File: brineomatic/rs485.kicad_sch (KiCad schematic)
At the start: 12 parts, among them J23 3.5mm, J24 3.5mm, U10 MAX3485

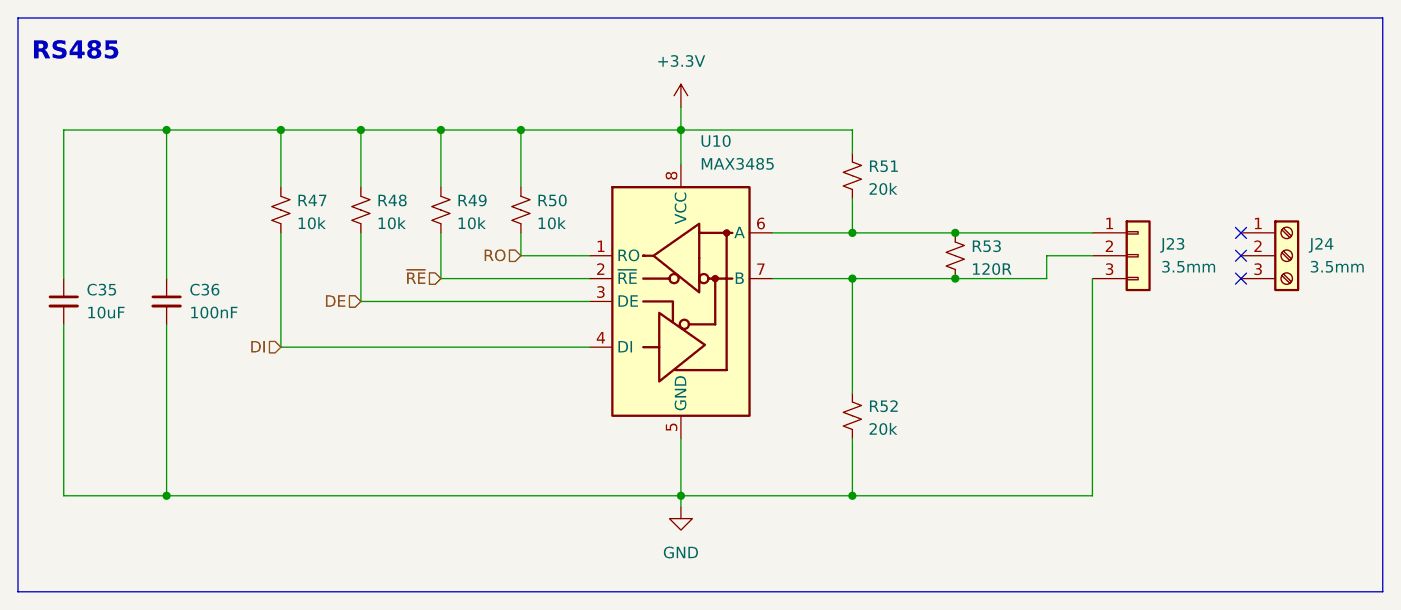
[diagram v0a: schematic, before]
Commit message: switch to rt7272b for 24v -> 5v regulator
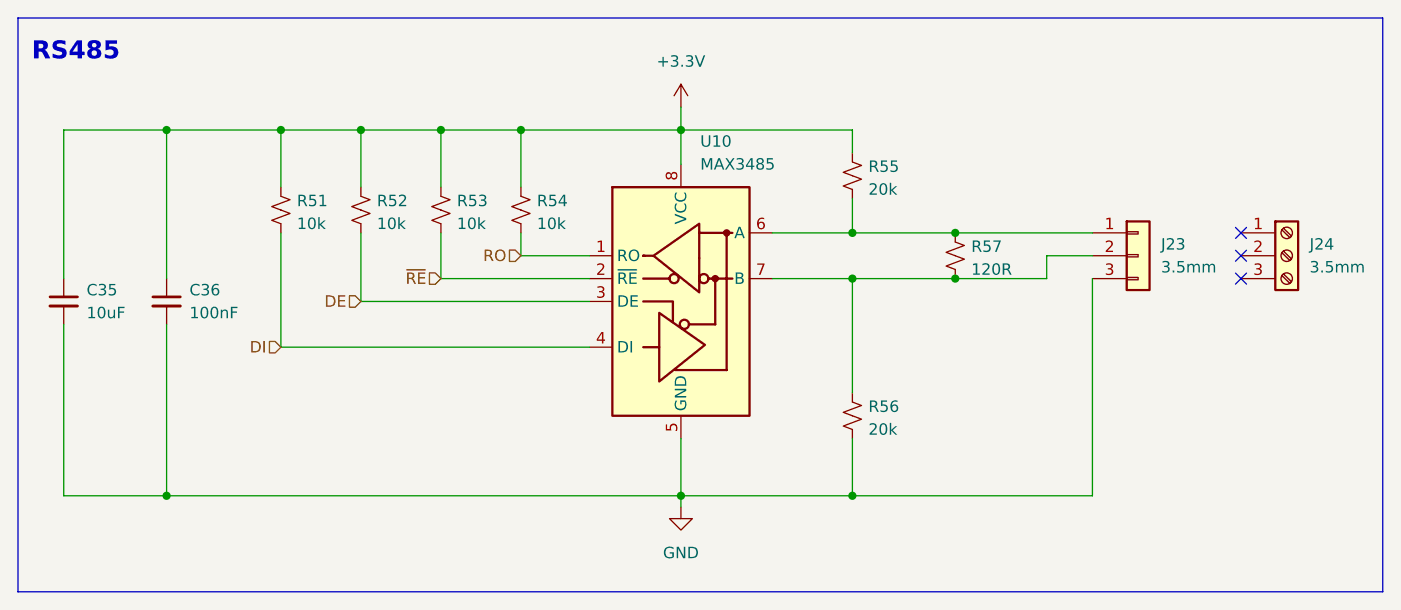
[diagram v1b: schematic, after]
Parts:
- renumbered R47 to R51, R48 to R52, R49 to R53, R50 to R54, R51 to R55, R52 to R56, R53 to R57
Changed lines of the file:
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@@
 		(dnp no)
 		(fields_autoplaced yes)
-		(property "Reference" "#PWR070"
+		(property "Reference" "#PWR068"
 			(at 140.97 130.81 0)
 			(effects
@@
 			(project "brineomatic"
 				(path "/96477ae2-ef08-48f3-8dd4-fe4478541f68/ecabf60a-7f79-4ba0-9fc6-a1e702c2d5f0"
-					(reference "#PWR070")
+					(reference "#PWR068")
 					(unit 1)
 				)
@@
 		(on_board yes)
 		(dnp no)
-		(property "Reference" "R52"
+		(property "Reference" "R56"
 			(at 161.798 113.284 0)
 			(effects
@@
 			(project "brineomatic"
 				(path "/96477ae2-ef08-48f3-8dd4-fe4478541f68/ecabf60a-7f79-4ba0-9fc6-a1e702c2d5f0"
-					(reference "R52")
+					(reference "R56")
 					(unit 1)
 				)
@@
 		(on_board yes)
 		(dnp no)
-		(property "Reference" "R47"
+		(property "Reference" "R51"
 			(at 98.298 90.424 0)
 			(effects
@@
 			(project "brineomatic"
 				(path "/96477ae2-ef08-48f3-8dd4-fe4478541f68/ecabf60a-7f79-4ba0-9fc6-a1e702c2d5f0"
-					(reference "R47")
+					(reference "R51")
 					(unit 1)
 				)
@@
 		(on_board yes)
 		(dnp no)
-		(property "Reference" "R49"
+		(property "Reference" "R53"
 			(at 116.078 90.424 0)
 			(effects
@@
 			(project "brineomatic"
 				(path "/96477ae2-ef08-48f3-8dd4-fe4478541f68/ecabf60a-7f79-4ba0-9fc6-a1e702c2d5f0"
-					(reference "R49")
+					(reference "R53")
 					(unit 1)
 				)
@@
 		(on_board yes)
 		(dnp no)
-		(property "Reference" "R50"
+		(property "Reference" "R54"
 			(at 124.968 90.424 0)
 			(effects
@@
 			(project "brineomatic"
 				(path "/96477ae2-ef08-48f3-8dd4-fe4478541f68/ecabf60a-7f79-4ba0-9fc6-a1e702c2d5f0"
-					(reference "R50")
+					(reference "R54")
 					(unit 1)
 				)
@@
 		(on_board yes)
 		(dnp no)
-		(property "Reference" "R53"
+		(property "Reference" "R57"
 			(at 173.228 95.504 0)
 			(effects
@@
 			(project "brineomatic"
 				(path "/96477ae2-ef08-48f3-8dd4-fe4478541f68/ecabf60a-7f79-4ba0-9fc6-a1e702c2d5f0"
-					(reference "R53")
+					(reference "R57")
 					(unit 1)
 				)
@@
 		(dnp no)
 		(fields_autoplaced yes)
-		(property "Reference" "#PWR069"
+		(property "Reference" "#PWR067"
 			(at 140.97 83.82 0)
 			(effects
@@
 			(project ""
 				(path "/96477ae2-ef08-48f3-8dd4-fe4478541f68/ecabf60a-7f79-4ba0-9fc6-a1e702c2d5f0"
-					(reference "#PWR069")
+					(reference "#PWR067")
 					(unit 1)
 				)
@@
 		(on_board yes)
 		(dnp no)
-		(property "Reference" "R48"
+		(property "Reference" "R52"
 			(at 107.188 90.424 0)
 			(effects
@@
 			(project "brineomatic"
 				(path "/96477ae2-ef08-48f3-8dd4-fe4478541f68/ecabf60a-7f79-4ba0-9fc6-a1e702c2d5f0"
-					(reference "R48")
+					(reference "R52")
 					(unit 1)
 				)
@@
 		(on_board yes)
 		(dnp no)
-		(property "Reference" "R51"
+		(property "Reference" "R55"
 			(at 161.798 86.614 0)
 			(effects
@@
 			(project "brineomatic"
 				(path "/96477ae2-ef08-48f3-8dd4-fe4478541f68/ecabf60a-7f79-4ba0-9fc6-a1e702c2d5f0"
-					(reference "R51")
-					(unit 1)
-				)
+					(reference "R55")
+					(unit 1)
+				)

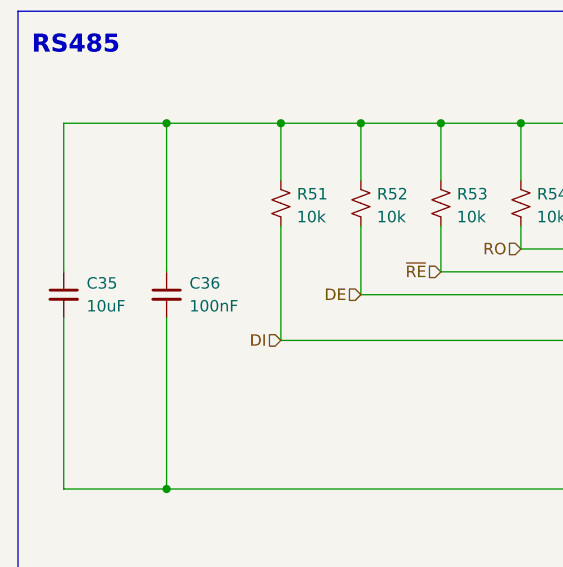
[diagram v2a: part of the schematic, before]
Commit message: added bulk cap to 5v rail and tidied silkscreen
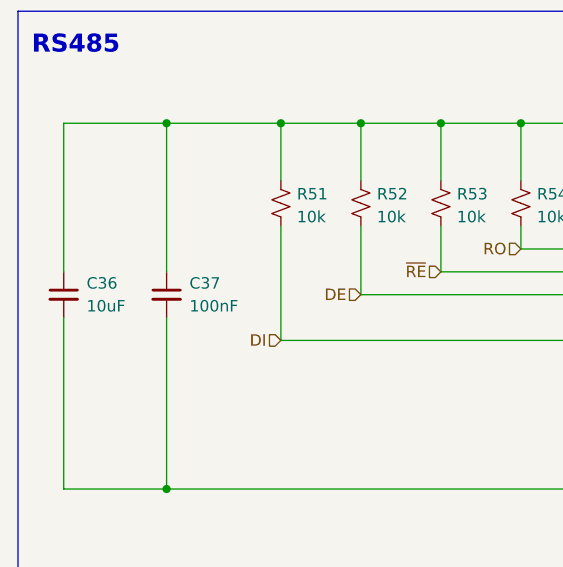
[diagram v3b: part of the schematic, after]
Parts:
- renumbered C35 to C36, C36 to C37
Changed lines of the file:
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@@
 		(on_board yes)
 		(dnp no)
-		(property "Reference" "C35"
+		(property "Reference" "C36"
 			(at 74.93 100.3363 0)
 			(effects
@@
 			(project "brineomatic"
 				(path "/96477ae2-ef08-48f3-8dd4-fe4478541f68/ecabf60a-7f79-4ba0-9fc6-a1e702c2d5f0"
-					(reference "C35")
+					(reference "C36")
 					(unit 1)
 				)
@@
 		(dnp no)
 		(fields_autoplaced yes)
-		(property "Reference" "C36"
+		(property "Reference" "C37"
 			(at 86.36 100.3363 0)
 			(effects
@@
 			(project "brineomatic"
 				(path "/96477ae2-ef08-48f3-8dd4-fe4478541f68/ecabf60a-7f79-4ba0-9fc6-a1e702c2d5f0"
-					(reference "C36")
-					(unit 1)
-				)
+					(reference "C37")
+					(unit 1)
+				)

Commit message: tested and update bom + placement
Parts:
- C37: LCSC (none) -> C14663
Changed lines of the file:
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@@
 			)
 		)
-		(property "LCSC" ""
+		(property "LCSC" "C14663"
 			(at 83.82 101.6 0)
 			(effects

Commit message: updated resistor p/ns in bom
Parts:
- R51, R52, R53, R54: LCSC (none) -> C25804
- R55, R56: LCSC (none) -> C4184
- R57: LCSC (none) -> C22787
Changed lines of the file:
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@@
+			)
+		)
+		(property "LCSC" " C4184"
+			(at 160.02 114.3 0)
+			(effects
+				(font
+					(size 1.27 1.27)
+				)
+				(hide yes)
 			)
 		)
@@
 			)
 		)
+		(property "LCSC" "C25804"
+			(at 96.52 91.44 0)
+			(effects
+				(font
+					(size 1.27 1.27)
+				)
+				(hide yes)
+			)
+		)
 		(pin "1"
 		)
@@
 			)
 		)
+		(property "LCSC" "C25804"
+			(at 114.3 91.44 0)
+			(effects
+				(font
+					(size 1.27 1.27)
+				)
+				(hide yes)
+			)
+		)
 		(pin "1"
 		)
@@
 			)
 		)
+		(property "LCSC" "C25804"
+			(at 123.19 91.44 0)
+			(effects
+				(font
+					(size 1.27 1.27)
+				)
+				(hide yes)
+			)
+		)
 		(pin "1"
 		)
@@
 		)
 		(property "Description" "Resistor, small US symbol"
+			(at 171.45 96.52 0)
+			(effects
+				(font
+					(size 1.27 1.27)
+				)
+				(hide yes)
+			)
+		)
+		(property "LCSC" " C22787"
 			(at 171.45 96.52 0)
 			(effects
@@
 			)
 		)
+		(property "LCSC" "C25804"
+			(at 105.41 91.44 0)
+			(effects
+				(font
+					(size 1.27 1.27)
+				)
+				(hide yes)
+			)
+		)
 		(pin "1"
 		)
@@
 			(at 160.02 87.63 0)
 			(effects
+				(font
+					(size 1.27 1.27)
+				)
+				(hide yes)
+			)
+		)
+		(property "LCSC" " C4184"
+			(at 160.02 87.63 0)
+			(effects

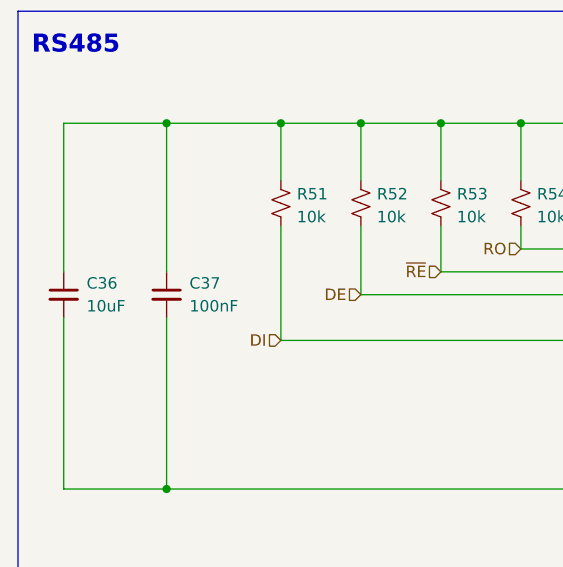
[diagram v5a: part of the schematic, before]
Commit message: added esd protection to relay driver connector
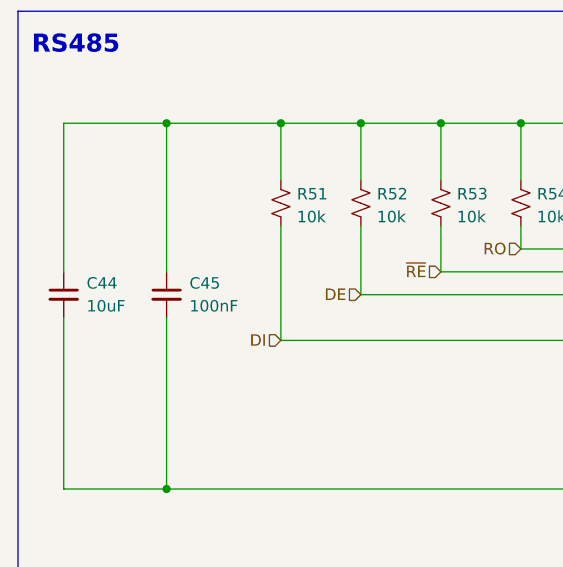
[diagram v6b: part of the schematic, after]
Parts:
- renumbered C36 to C44, C37 to C45
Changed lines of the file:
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@@
 		(on_board yes)
 		(dnp no)
-		(property "Reference" "C36"
+		(property "Reference" "C44"
 			(at 74.93 100.3363 0)
 			(effects
@@
 			(project "brineomatic"
 				(path "/96477ae2-ef08-48f3-8dd4-fe4478541f68/ecabf60a-7f79-4ba0-9fc6-a1e702c2d5f0"
-					(reference "C36")
+					(reference "C44")
 					(unit 1)
 				)
@@
 		(dnp no)
 		(fields_autoplaced yes)
-		(property "Reference" "C37"
+		(property "Reference" "C45"
 			(at 86.36 100.3363 0)
 			(effects
@@
 			(project "brineomatic"
 				(path "/96477ae2-ef08-48f3-8dd4-fe4478541f68/ecabf60a-7f79-4ba0-9fc6-a1e702c2d5f0"
-					(reference "C37")
-					(unit 1)
-				)
+					(reference "C45")
+					(unit 1)
+				)

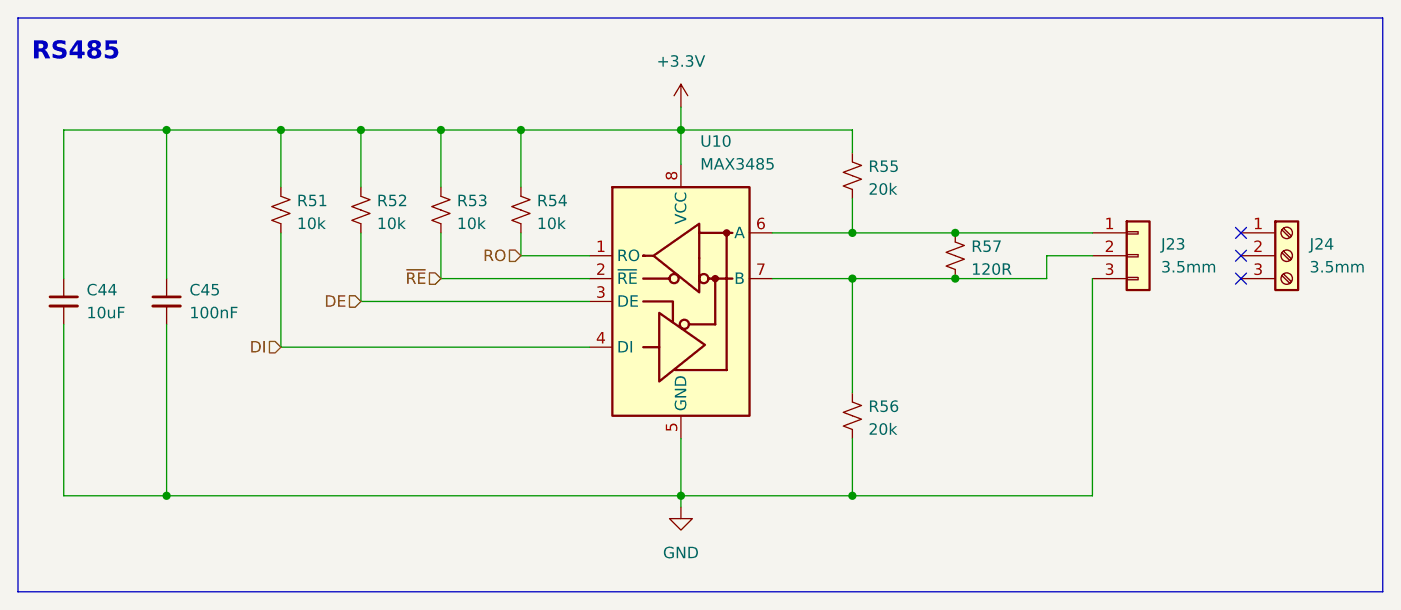
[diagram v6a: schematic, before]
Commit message: put 2x0 ohm between GND and USB SHIELD
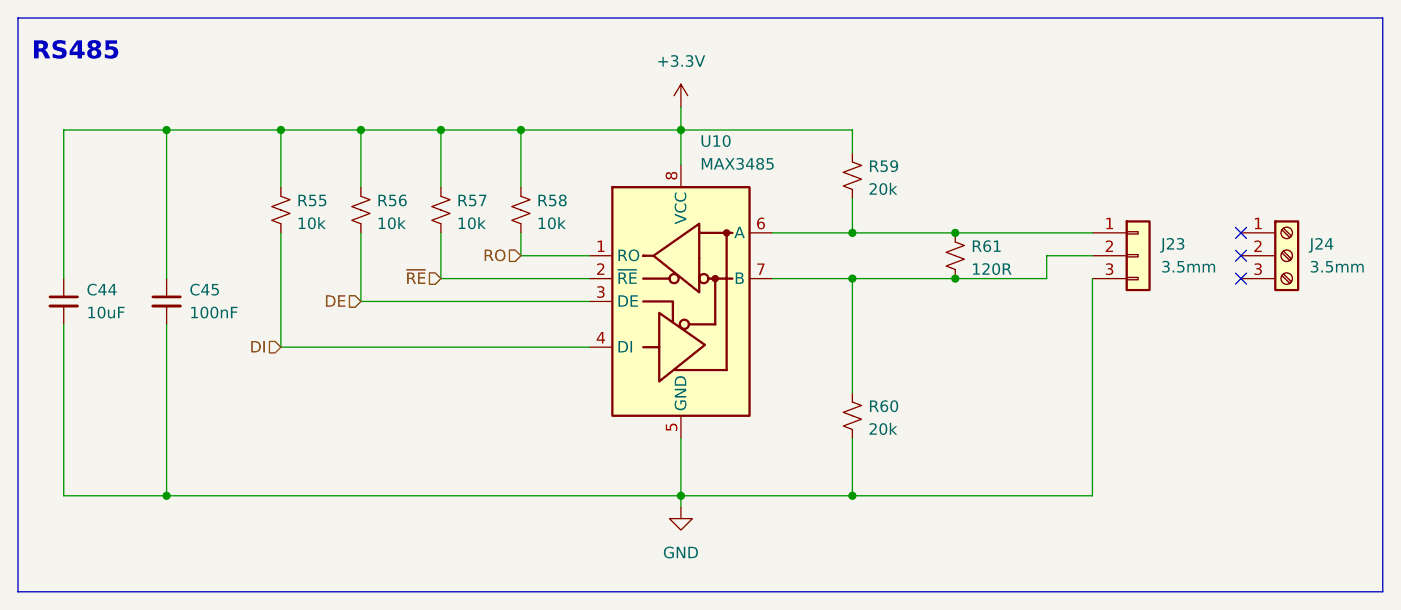
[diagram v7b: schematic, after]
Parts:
- renumbered R51 to R55, R52 to R56, R53 to R57, R54 to R58, R55 to R59, R56 to R60, R57 to R61
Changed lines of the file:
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@@
 		(on_board yes)
 		(dnp no)
-		(property "Reference" "R56"
+		(property "Reference" "R60"
 			(at 161.798 113.284 0)
 			(effects
@@
 			(project "brineomatic"
 				(path "/96477ae2-ef08-48f3-8dd4-fe4478541f68/ecabf60a-7f79-4ba0-9fc6-a1e702c2d5f0"
-					(reference "R56")
+					(reference "R60")
 					(unit 1)
 				)
@@
 		(on_board yes)
 		(dnp no)
-		(property "Reference" "R51"
+		(property "Reference" "R55"
 			(at 98.298 90.424 0)
 			(effects
@@
 			(project "brineomatic"
 				(path "/96477ae2-ef08-48f3-8dd4-fe4478541f68/ecabf60a-7f79-4ba0-9fc6-a1e702c2d5f0"
-					(reference "R51")
+					(reference "R55")
 					(unit 1)
 				)
@@
 		(on_board yes)
 		(dnp no)
-		(property "Reference" "R53"
+		(property "Reference" "R57"
 			(at 116.078 90.424 0)
 			(effects
@@
 			(project "brineomatic"
 				(path "/96477ae2-ef08-48f3-8dd4-fe4478541f68/ecabf60a-7f79-4ba0-9fc6-a1e702c2d5f0"
-					(reference "R53")
+					(reference "R57")
 					(unit 1)
 				)
@@
 		(on_board yes)
 		(dnp no)
-		(property "Reference" "R54"
+		(property "Reference" "R58"
 			(at 124.968 90.424 0)
 			(effects
@@
 			(project "brineomatic"
 				(path "/96477ae2-ef08-48f3-8dd4-fe4478541f68/ecabf60a-7f79-4ba0-9fc6-a1e702c2d5f0"
-					(reference "R54")
+					(reference "R58")
 					(unit 1)
 				)
@@
 		(on_board yes)
 		(dnp no)
-		(property "Reference" "R57"
+		(property "Reference" "R61"
 			(at 173.228 95.504 0)
 			(effects
@@
 			(project "brineomatic"
 				(path "/96477ae2-ef08-48f3-8dd4-fe4478541f68/ecabf60a-7f79-4ba0-9fc6-a1e702c2d5f0"
-					(reference "R57")
+					(reference "R61")
 					(unit 1)
 				)
@@
 		(on_board yes)
 		(dnp no)
-		(property "Reference" "R52"
+		(property "Reference" "R56"
 			(at 107.188 90.424 0)
 			(effects
@@
 			(project "brineomatic"
 				(path "/96477ae2-ef08-48f3-8dd4-fe4478541f68/ecabf60a-7f79-4ba0-9fc6-a1e702c2d5f0"
-					(reference "R52")
+					(reference "R56")
 					(unit 1)
 				)
@@
 		(on_board yes)
 		(dnp no)
-		(property "Reference" "R55"
+		(property "Reference" "R59"
 			(at 161.798 86.614 0)
 			(effects
@@
 			(project "brineomatic"
 				(path "/96477ae2-ef08-48f3-8dd4-fe4478541f68/ecabf60a-7f79-4ba0-9fc6-a1e702c2d5f0"
-					(reference "R55")
-					(unit 1)
-				)
+					(reference "R59")
+					(unit 1)
+				)

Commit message: add ESD and series resistor to GPIO0/EN
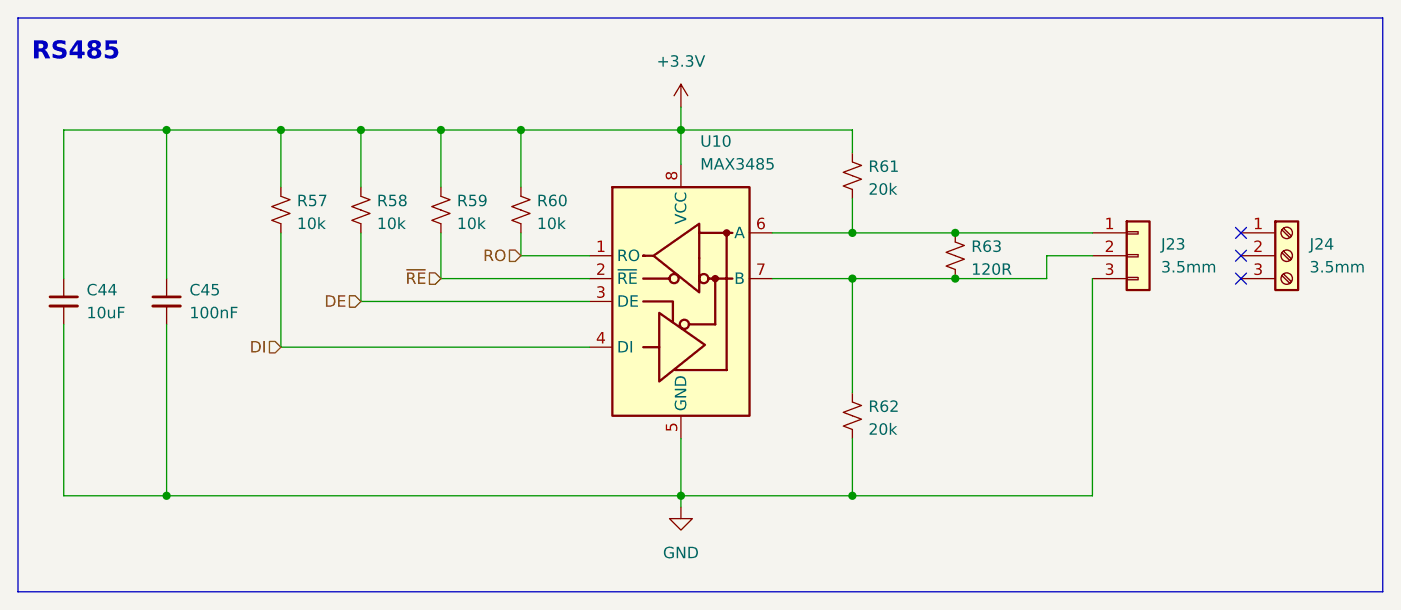
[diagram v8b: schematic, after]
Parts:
- renumbered R55 to R57, R56 to R58, R57 to R59, R58 to R60, R59 to R61, R60 to R62, R61 to R63
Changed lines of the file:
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@@
 		(on_board yes)
 		(dnp no)
-		(property "Reference" "R60"
+		(property "Reference" "R62"
 			(at 161.798 113.284 0)
 			(effects
@@
 			(project "brineomatic"
 				(path "/96477ae2-ef08-48f3-8dd4-fe4478541f68/ecabf60a-7f79-4ba0-9fc6-a1e702c2d5f0"
-					(reference "R60")
+					(reference "R62")
 					(unit 1)
 				)
@@
 		(on_board yes)
 		(dnp no)
-		(property "Reference" "R55"
+		(property "Reference" "R57"
 			(at 98.298 90.424 0)
 			(effects
@@
 			(project "brineomatic"
 				(path "/96477ae2-ef08-48f3-8dd4-fe4478541f68/ecabf60a-7f79-4ba0-9fc6-a1e702c2d5f0"
-					(reference "R55")
+					(reference "R57")
 					(unit 1)
 				)
@@
 		(on_board yes)
 		(dnp no)
-		(property "Reference" "R57"
+		(property "Reference" "R59"
 			(at 116.078 90.424 0)
 			(effects
@@
 			(project "brineomatic"
 				(path "/96477ae2-ef08-48f3-8dd4-fe4478541f68/ecabf60a-7f79-4ba0-9fc6-a1e702c2d5f0"
-					(reference "R57")
+					(reference "R59")
 					(unit 1)
 				)
@@
 		(on_board yes)
 		(dnp no)
-		(property "Reference" "R58"
+		(property "Reference" "R60"
 			(at 124.968 90.424 0)
 			(effects
@@
 			(project "brineomatic"
 				(path "/96477ae2-ef08-48f3-8dd4-fe4478541f68/ecabf60a-7f79-4ba0-9fc6-a1e702c2d5f0"
-					(reference "R58")
+					(reference "R60")
 					(unit 1)
 				)
@@
 		(on_board yes)
 		(dnp no)
-		(property "Reference" "R61"
+		(property "Reference" "R63"
 			(at 173.228 95.504 0)
 			(effects
@@
 			(project "brineomatic"
 				(path "/96477ae2-ef08-48f3-8dd4-fe4478541f68/ecabf60a-7f79-4ba0-9fc6-a1e702c2d5f0"
-					(reference "R61")
+					(reference "R63")
 					(unit 1)
 				)
@@
 		(on_board yes)
 		(dnp no)
-		(property "Reference" "R56"
+		(property "Reference" "R58"
 			(at 107.188 90.424 0)
 			(effects
@@
 			(project "brineomatic"
 				(path "/96477ae2-ef08-48f3-8dd4-fe4478541f68/ecabf60a-7f79-4ba0-9fc6-a1e702c2d5f0"
-					(reference "R56")
+					(reference "R58")
 					(unit 1)
 				)
@@
 		(on_board yes)
 		(dnp no)
-		(property "Reference" "R59"
+		(property "Reference" "R61"
 			(at 161.798 86.614 0)
 			(effects
@@
 			(project "brineomatic"
 				(path "/96477ae2-ef08-48f3-8dd4-fe4478541f68/ecabf60a-7f79-4ba0-9fc6-a1e702c2d5f0"
-					(reference "R59")
-					(unit 1)
-				)
+					(reference "R61")
+					(unit 1)
+				)
